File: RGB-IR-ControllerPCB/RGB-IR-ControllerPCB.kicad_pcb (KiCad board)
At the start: 2 copper layers, 63 x 63 mm, 16 parts, among them J1 Conn_01x02_Female, J2 Conn_01x01_Female, J3 Conn_01x01_Female, J4 Conn_01x01_Female, J5 Conn_01x01_Female, Q1 IRF540N, Q2 IRF540N, Q3 IRF540N, U1 TSOP17xx

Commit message: Updated PCB and clear deprecate code
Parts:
- removed J3, J4, J5: Conn_01x01_Female, Connector_Pin:Pin_D1.4mm_L8.5mm_W2.8mm_FlatFork
- A1, U1: moved to B.Cu
- J1: value Conn_01x02_Female -> Screw_Terminal_01x02; footprint TerminalBlock:TerminalBlock_bornier-2_P5.08mm -> TerminalBlock:TerminalBlock_Altech_AK300-2_P5.00mm; moved to B.Cu
- J2: value Conn_01x01_Female -> Screw_Terminal_01x04; footprint Connector_Pin:Pin_D1.4mm_L8.5mm_W2.8mm_FlatFork -> TerminalBlock:TerminalBlock_Altech_AK300-4_P5.00mm; moved to B.Cu
- moved J1 57.0 mm to (43.0, 77.5)
- moved U1 50.9 mm to (27.9, 78.7)
- moved A1 44.8 mm to (24.1, 64.8)
- moved J2 44.6 mm to (75.6, 60.3), turned to 90 degrees
- moved Q3 40.6 mm to (60.8, 38.5), turned to 0 degrees
- moved R5 38.0 mm to (52.8, 36.5), turned to 0 degrees
- moved R6 34.2 mm to (52.8, 40.5), turned to 0 degrees
- moved Q2 22.1 mm to (60.8, 47.0), turned to 0 degrees
- moved Q1 21.8 mm to (60.8, 55.5), turned to 0 degrees
- moved R3 13.5 mm to (52.8, 45.0), turned to 0 degrees
- moved R1 13.0 mm to (52.8, 53.5), turned to 0 degrees
- moved R4 10.1 mm to (52.8, 49.0), turned to 0 degrees
- moved R2 9.51 mm to (52.8, 57.5), turned to 0 degrees
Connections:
- A1 pad 1: (no net) -> Net-(A1-Pad1)
- A1 pad 10: (no net) -> Net-(A1-Pad10)
- A1 pad 11: (no net) -> Net-(A1-Pad11)
- A1 pad 12: RED_PIN -> GREEN_PIN
- A1 pad 13: GREEN_PIN -> RED_PIN
- A1 pad 15: (no net) -> Net-(A1-Pad15)
- A1 pad 16: (no net) -> Net-(A1-Pad16)
- A1 pad 17: (no net) -> Net-(A1-Pad17)
- A1 pad 18: (no net) -> Net-(A1-Pad18)
- A1 pad 19: (no net) -> Net-(A1-Pad19)
- A1 pad 2: (no net) -> Net-(A1-Pad2)
- A1 pad 20: (no net) -> Net-(A1-Pad20)
- A1 pad 21: (no net) -> Net-(A1-Pad21)
- A1 pad 22: (no net) -> Net-(A1-Pad22)
- A1 pad 23: (no net) -> Net-(A1-Pad23)
- A1 pad 24: (no net) -> Net-(A1-Pad24)
- A1 pad 25: (no net) -> Net-(A1-Pad25)
- A1 pad 26: (no net) -> Net-(A1-Pad26)
- A1 pad 28: (no net) -> Net-(A1-Pad28)
- A1 pad 3: (no net) -> Net-(A1-Pad3)
- A1 pad 6: (no net) -> Net-(A1-Pad6)
- A1 pad 7: (no net) -> Net-(A1-Pad7)
- A1 pad 8: (no net) -> Net-(A1-Pad8)
- A1 pad 9: (no net) -> Net-(A1-Pad9)
- Q1 pad 2: Net-(J3-Pad1) -> Net-(J2-Pad2)
- Q2 pad 2: Net-(J4-Pad1) -> Net-(J2-Pad3)
- Q3 pad 2: Net-(J5-Pad1) -> Net-(J2-Pad4)
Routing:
- net GREEN_PIN: track 4.51 -> 60.7 mm
- net RED_PIN: track 8.80 -> 54.2 mm
- net BLUE_PIN: track 8.53 -> 47.2 mm
- net Net-(J2-Pad2): track 0.00 -> 15.6 mm
- net Net-(J2-Pad4): track 0.00 -> 15.5 mm
- net Net-(J2-Pad3): track 0.00 -> 14.0 mm
- net IR_DATA_OUT: track 40.9 -> 27.2 mm
- net Net-(J3-Pad1): track 9.80 -> 0.00 mm
- net +5V: track 37.0 -> 28.5 mm
- net Net-(J5-Pad1): track 6.90 -> 0.00 mm
- net Net-(J4-Pad1): track 6.84 -> 0.00 mm
- net +12V: track 59.3 -> 61.4 mm
- net Net-(Q3-Pad1): track 6.92 -> 8.33 mm
- net Net-(Q1-Pad1): track 7.02 -> 7.74 mm

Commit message: Refactored PCB
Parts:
- moved U1 107.6 mm to (135.5, 79.0)
- moved A1 100.5 mm to (124.5, 70.0)
- moved J1 94.1 mm to (119.8, 23.0)
- moved R5 69.5 mm to (119.0, 57.8), turned to 270 degrees
- moved R6 64.5 mm to (115.0, 57.8), turned to 270 degrees
- moved Q3 62.5 mm to (117.0, 65.8), turned to 270 degrees
- moved R3 59.1 mm to (110.5, 57.8), turned to 270 degrees
- moved R4 54.4 mm to (106.5, 57.8), turned to 270 degrees
- moved Q2 51.2 mm to (108.5, 65.8), turned to 270 degrees
- moved R1 49.4 mm to (102.0, 57.8), turned to 270 degrees
- moved R2 45.2 mm to (98.0, 57.8), turned to 270 degrees
- moved Q1 40.5 mm to (100.0, 65.8), turned to 270 degrees
- moved J2 29.7 mm to (97.8, 80.0), turned to 0 degrees
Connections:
- A1 pad 12: GREEN_PIN -> BLUE_PIN
- A1 pad 14: BLUE_PIN -> GREEN_PIN
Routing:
- net +12V: track 61.4 -> 147.1 mm
- net BLUE_PIN: track 47.2 -> 18.9 mm
- net RED_PIN: track 54.2 -> 26.1 mm
- net GREEN_PIN: track 60.7 -> 33.6 mm
- net IR_DATA_OUT: track 27.2 -> 21.3 mm
- net +5V: track 28.5 -> 25.6 mm
- net Net-(J2-Pad3): track 14.0 -> 12.4 mm
- net Net-(J2-Pad4): track 15.5 -> 13.8 mm
- net Net-(Q2-Pad1): track 7.75 -> 6.53 mm
- net Net-(Q3-Pad1): track 8.33 -> 7.35 mm
- net Net-(Q1-Pad1): track 7.74 -> 6.92 mm
- net Net-(J2-Pad2): track 15.6 -> 16.4 mm
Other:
- board size 63 x 63 mm -> 52.5 x 64.5 mm

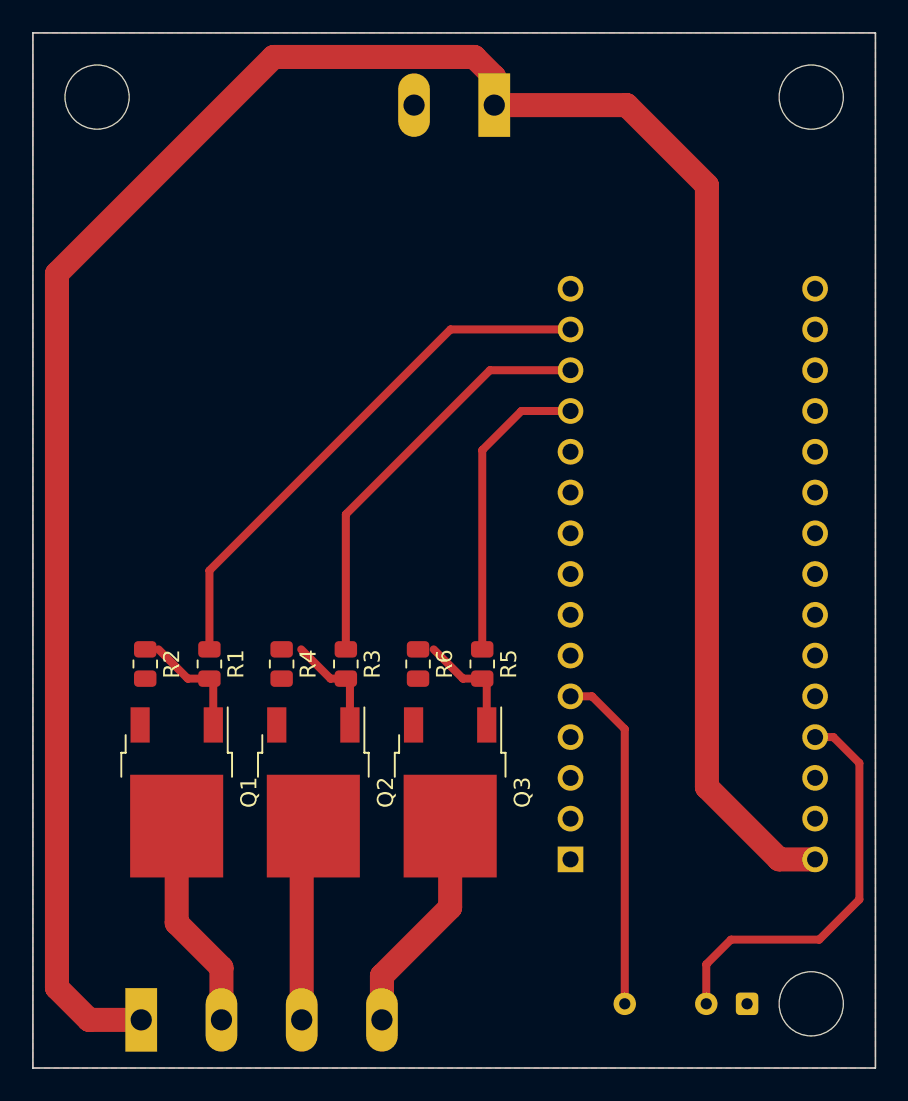
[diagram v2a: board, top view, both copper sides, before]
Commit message: updated pcb smd resistors to tht
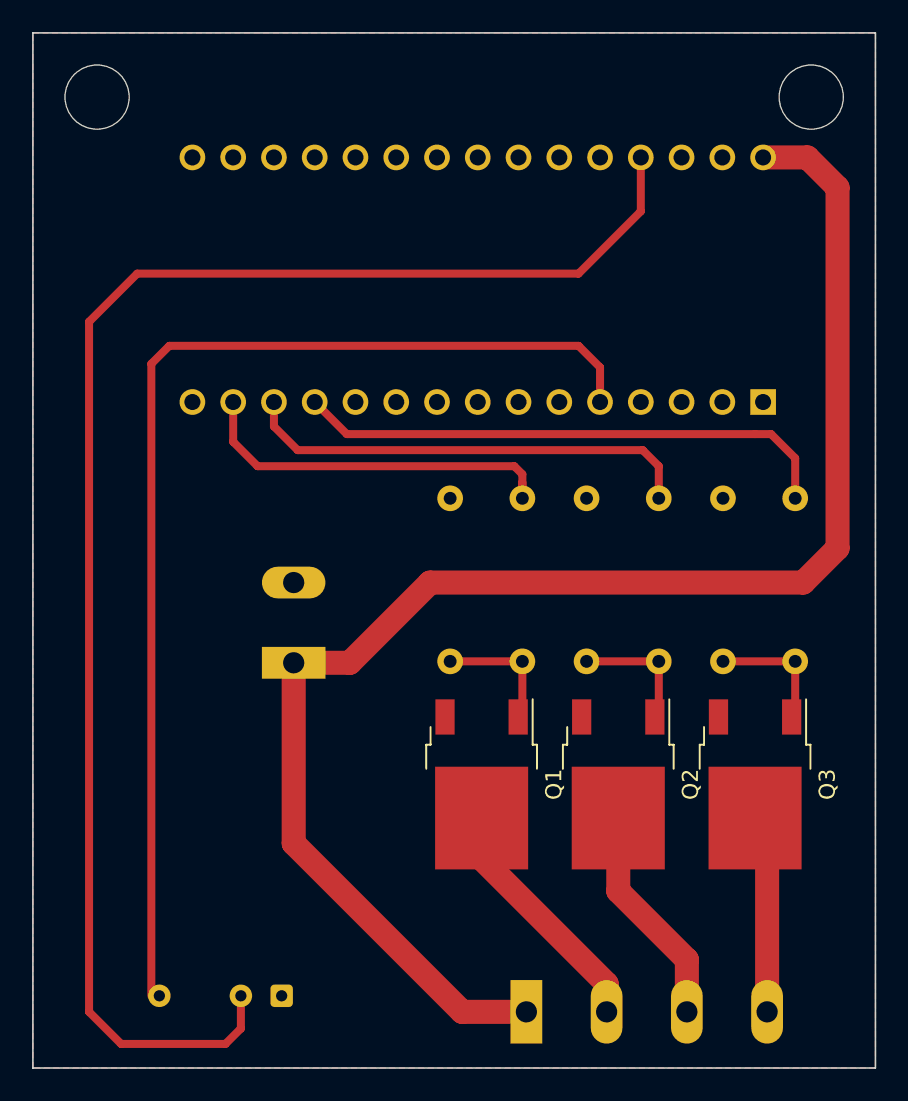
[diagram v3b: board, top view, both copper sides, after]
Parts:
- R1, R2, R3, R4, R5, R6: footprint Resistor_SMD:R_0805_2012Metric -> Resistor_THT:R_Axial_DIN0207_L6.3mm_D2.5mm_P10.16mm_Horizontal; moved to B.Cu
- moved J1 36.9 mm to (107.2, 57.8), turned to 90 degrees
- moved A1 30.9 mm to (136.5, 41.5), turned to 90 degrees
- moved U1 29.0 mm to (106.5, 78.5)
- moved J2 24.0 mm to (121.8, 79.5)
- moved R1 22.1 mm to (121.5, 47.5)
- moved R3 22.1 mm to (130.0, 47.5)
- moved R5 22.1 mm to (138.5, 47.5)
- moved R2 21.6 mm to (117.0, 47.5)
- moved R4 21.6 mm to (125.5, 47.5)
- moved R6 21.6 mm to (134.0, 47.5)
- moved Q1 19.0 mm to (119.0, 65.3)
- moved Q2 19.0 mm to (127.5, 65.3)
- moved Q3 19.0 mm to (136.0, 65.3)
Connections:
- A1 pad 1: Net-(A1-Pad1) -> (no net)
- A1 pad 10: Net-(A1-Pad10) -> (no net)
- A1 pad 11: Net-(A1-Pad11) -> (no net)
- A1 pad 15: Net-(A1-Pad15) -> (no net)
- A1 pad 16: Net-(A1-Pad16) -> (no net)
- A1 pad 17: Net-(A1-Pad17) -> (no net)
- A1 pad 18: Net-(A1-Pad18) -> (no net)
- A1 pad 19: Net-(A1-Pad19) -> (no net)
- A1 pad 2: Net-(A1-Pad2) -> (no net)
- A1 pad 20: Net-(A1-Pad20) -> (no net)
- A1 pad 21: Net-(A1-Pad21) -> (no net)
- A1 pad 22: Net-(A1-Pad22) -> (no net)
- A1 pad 23: Net-(A1-Pad23) -> (no net)
- A1 pad 24: Net-(A1-Pad24) -> (no net)
- A1 pad 25: Net-(A1-Pad25) -> (no net)
- A1 pad 26: Net-(A1-Pad26) -> (no net)
- A1 pad 28: Net-(A1-Pad28) -> (no net)
- A1 pad 3: Net-(A1-Pad3) -> (no net)
- A1 pad 6: Net-(A1-Pad6) -> (no net)
- A1 pad 7: Net-(A1-Pad7) -> (no net)
- A1 pad 8: Net-(A1-Pad8) -> (no net)
- A1 pad 9: Net-(A1-Pad9) -> (no net)
- R2 pad 1: Net-(Q1-Pad1) -> GND
- R2 pad 2: GND -> Net-(Q1-Pad1)
- R4 pad 1: Net-(Q2-Pad1) -> GND
- R4 pad 2: GND -> Net-(Q2-Pad1)
- R6 pad 1: Net-(Q3-Pad1) -> GND
- R6 pad 2: GND -> Net-(Q3-Pad1)
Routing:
- net +5V: track 25.6 -> 96.3 mm
- net +12V: track 147.1 -> 94.8 mm
- net IR_DATA_OUT: track 21.3 -> 70.5 mm
- net BLUE_PIN: track 18.9 -> 33.9 mm
- net GREEN_PIN: track 33.6 -> 23.8 mm
- net RED_PIN: track 26.1 -> 28.5 mm
- net Net-(J2-Pad2): track 16.4 -> 18.5 mm
- net Net-(Q2-Pad1): track 6.53 -> 8.41 mm
- net Net-(J2-Pad3): track 12.4 -> 13.8 mm
- net Net-(J2-Pad4): track 13.8 -> 12.4 mm
- net Net-(Q1-Pad1): track 6.92 -> 8.07 mm
- net Net-(Q3-Pad1): track 7.35 -> 8.06 mm
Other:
- outline, holes or cut-outs redrawn

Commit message: Added 5V Voltage Regulator
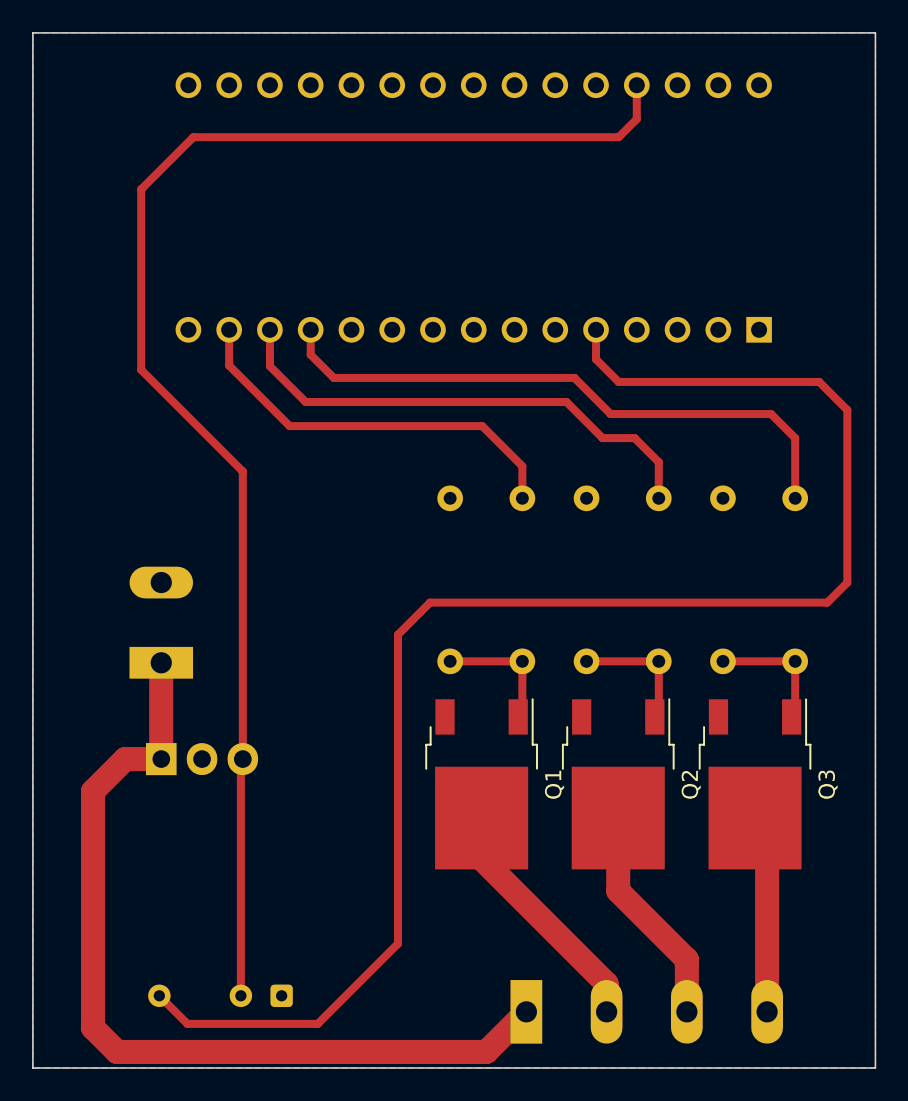
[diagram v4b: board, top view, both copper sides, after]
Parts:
- added U2: L7805, Package_TO_SOT_THT:TO-220-3_Vertical, B.Cu at (99.0, 63.8)
- moved J1 8.25 mm to (99.0, 57.8)
- moved A1 4.51 mm to (136.2, 37.0)
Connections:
- A1 pad 30: +12V -> (no net)
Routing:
- net +12V: track 94.8 -> 54.5 mm
- net IR_DATA_OUT: track 70.5 -> 95.8 mm
- net +5V: track 96.3 -> 87.7 mm
- net BLUE_PIN: track 33.9 -> 37.6 mm
- net RED_PIN: track 28.5 -> 31.2 mm
- net GREEN_PIN: track 23.8 -> 25.1 mm
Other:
- outline, holes or cut-outs redrawn
